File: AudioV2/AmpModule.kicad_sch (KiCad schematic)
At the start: 26 parts, among them J701 AMP_IN L/R, J702 AMP_OUT L/R, J703 +12V / A_GND / -12V

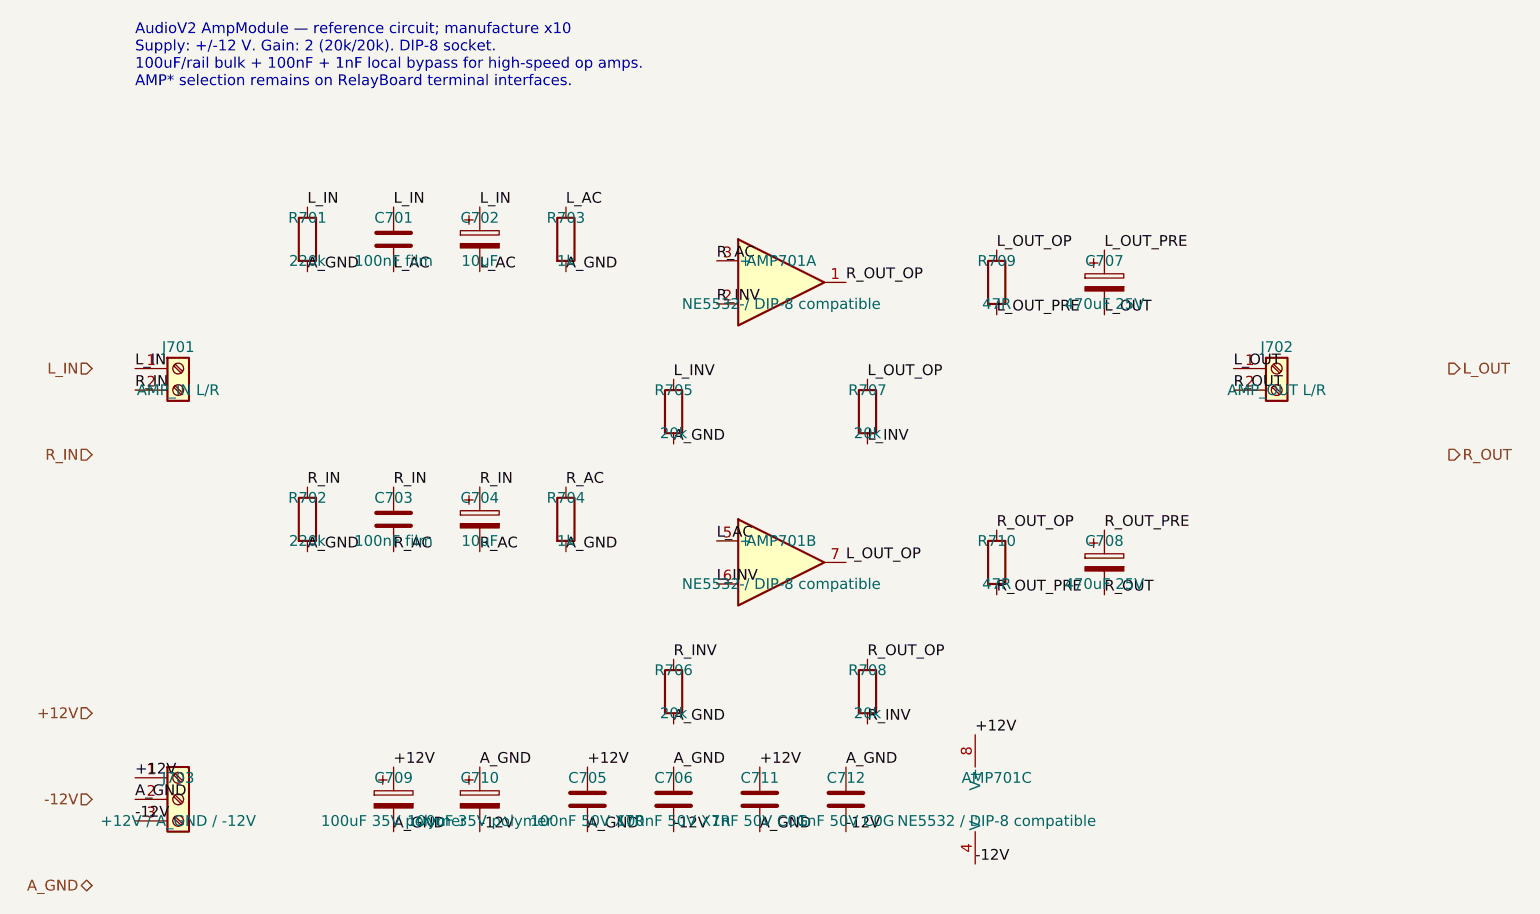
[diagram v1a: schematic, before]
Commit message: AudioV2: regenerate AmpModule and clear hierarchical label dangling
Colocate net_at on the seven hierarchical ports (OutputStage pattern),
run wire_circuit_design.py amp under KiCad 10.0.6, and record ERC
verification in AGENT_HANDOFF (Amp hier dangling 7→0).

Co-authored-by: m_arino <indare@users.noreply.github.com>
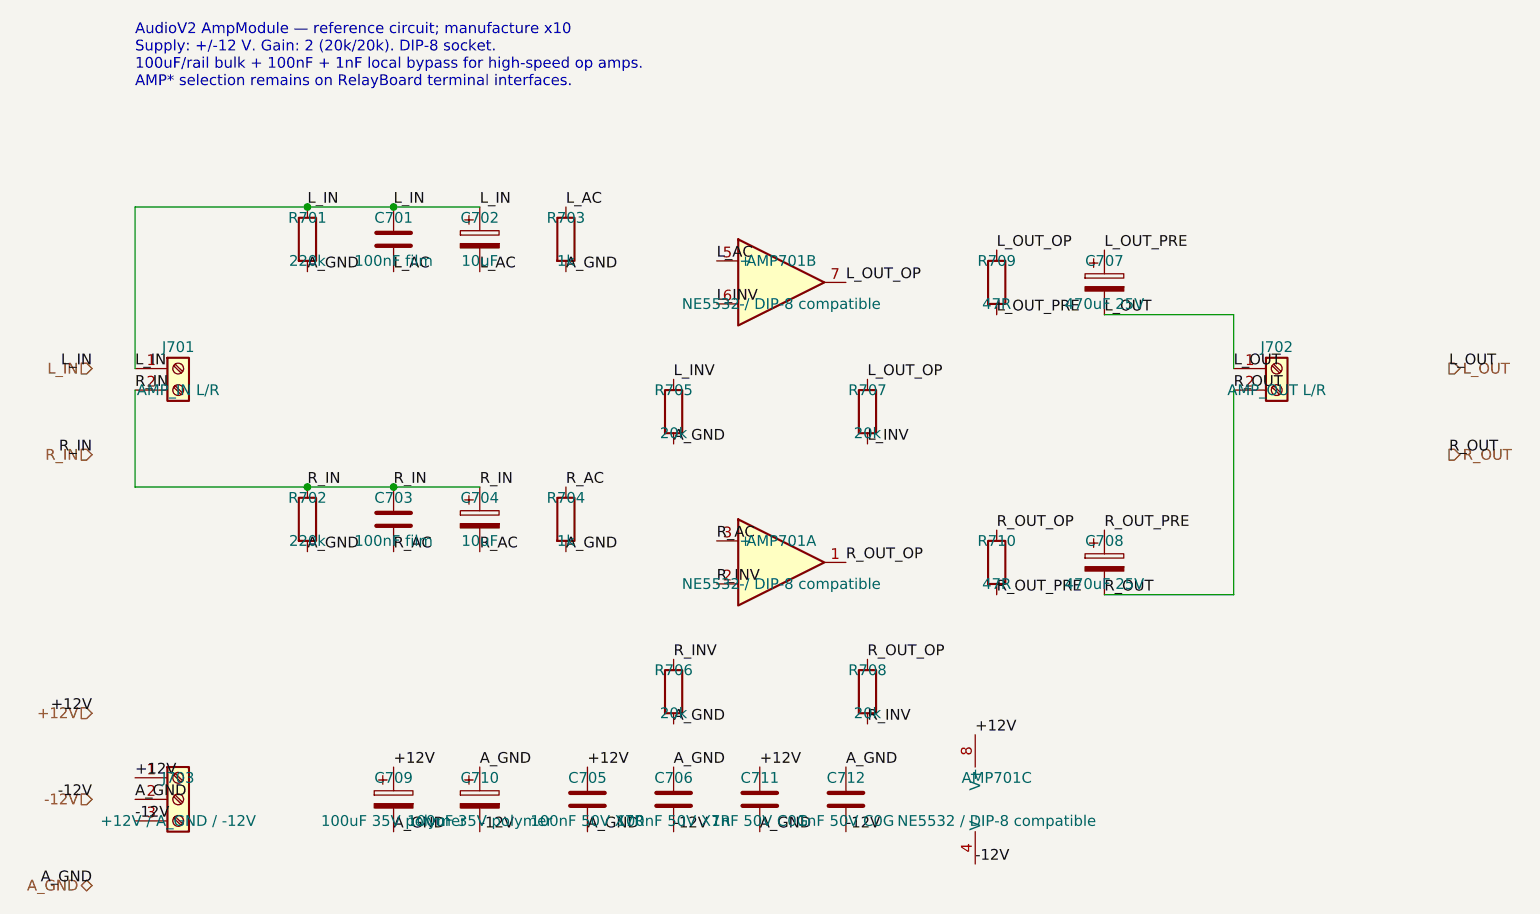
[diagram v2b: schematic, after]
